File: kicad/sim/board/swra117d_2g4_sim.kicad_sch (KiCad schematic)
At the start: 2 parts, among them P1 50R port

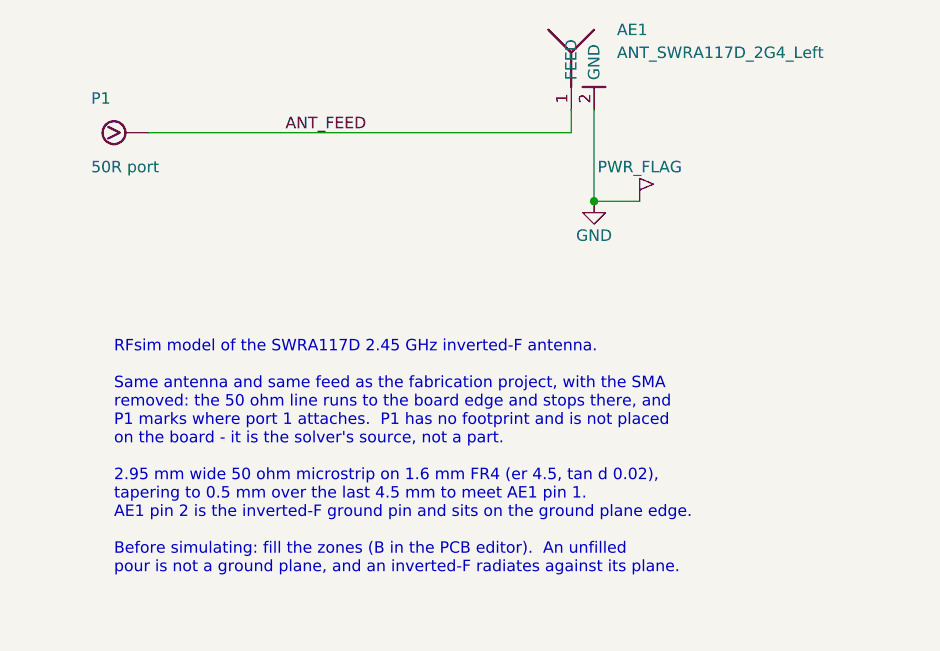
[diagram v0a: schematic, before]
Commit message: Give the RFsim port a pad with reference copper under it
RFsim reported, on the previous version:

    Port 1 (AE1 Pad 1 (ANT_FEED)): no copper on reference layer B.Cu under
    the pad.

Two things behind it, and the first one was my mistake.  RFsim attaches its
port to a *pad*, not to a track end, so removing the connector left the board
with no pad at the launch and RFsim fell back to the antenna's own feed pad -
which sits on the ground plane edge with the keep-out above it and has no
plane beneath it by design.  A bare track end was never going to work.

So the connector is replaced by a bare port land rather than by nothing:

  * RF_Port_Land - the signal pad, the width of the 50 ohm line, with a solid
    B.Cu ground pad directly under it.  Generated by gen_sma_footprint.py
    --style port, from the same code and the same stackup as the SMA land, so
    the only electrical difference between the two boards is the thing being
    measured.
  * No coplanar ground tabs.  That is what keeps the line a plain microstrip,
    and it is why MSL is the right port model here where CPW is right on the
    fabrication board.  check_sim_board.py fails if anyone adds an F.Cu ground
    pad back, because that silently invalidates the port model the docs tell
    you to use.
  * The reference is a pad, not a zone.  Zones ship unfilled, so a reference
    that waits on a fill is a reference that is missing the first time the
    project is opened - which is the second half of the reported error.

RF_PORT gains a ground pin and the RF_Port_Land footprint; P1 is now a real
board part rather than a sheet-only symbol.  The feed line ends on the port
pad instead of the board edge.  Launch vias sit inside the land's ground pad.

Also fixed: gen_sma_footprint.py derived three uuids from hash(), which
Python salts per process, so the footprint came out different on every run.
Numbered instead.  The fabrication board changes by three uuids and no
geometry.

check_sim_board.py grows t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
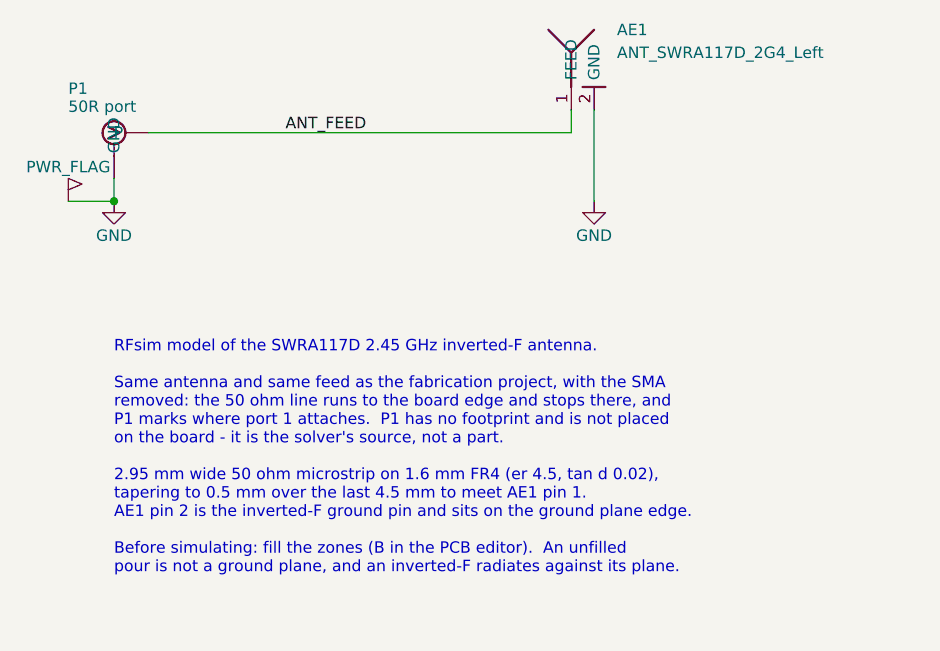
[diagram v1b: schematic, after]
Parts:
- P1: footprint (none) -> SWRA117D_RF:RF_Port_Land
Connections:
- net GND: now also P1.2 (GND)
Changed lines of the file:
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@@
+	)
+	(wire
+		(pts (xy 76.2 93.98) (xy 76.2 96.52))
+		(stroke (width 0) (type default))
+	)
+	(wire
+		(pts (xy 76.2 96.52) (xy 71.12 96.52))
+		(stroke (width 0) (type default))
 	)
 	(wire
@@
 		(stroke (width 0) (type default))
 	)
-	(wire
-		(pts (xy 129.54 96.52) (xy 134.62 96.52))
-		(stroke (width 0) (type default))
-	)
 	(junction
-		(at 129.54 96.52)
+		(at 76.2 96.52)
 		(diameter 0)
 		(color 0 0 0 0)
@@
 		(exclude_from_sim no)
 		(in_bom no)
-		(on_board no)
+		(on_board yes)
 		(dnp no)
-		(property "Reference" "P1"
-			(at 73.66 85.09 0)
-			(effects (font (size 1.27 1.27)) (justify left))
+		(property "Reference" "P1" (at 71.12 84 0) (effects (font (size 1.27 1.27)) (justify left)))
+		(property "Value" "50R port" (at 71.12 86 0) (effects (font (size 1.27 1.27)) (justify left)))
+		(property "Footprint" "SWRA117D_RF:RF_Port_Land"
+			(at 76.2 88.9 0)
+			(effects (font (size 1.27 1.27)) (hide yes))
 		)
-		(property "Value" "50R port"
-			(at 73.66 92.71 0)
-			(effects (font (size 1.27 1.27)) (justify left))
-		)
-		(property "Footprint" "" (at 76.2 88.9 0) (effects (font (size 1.27 1.27)) (hide yes)))
 		(property "Datasheet" "~" (at 76.2 88.9 0) (effects (font (size 1.27 1.27)) (hide yes)))
-		(property "Description" "50 ohm simulation port - attach RFsim port 1 to the feed track where it meets the board edge"
+		(property "Description" "50 ohm board-edge port land - attach RFsim port 1 to pad 1, with pad 2 on B.Cu as its reference"
 			(at 76.2 88.9 0)
 			(effects (font (size 1.27 1.27)) (hide yes))
 		)
 		(pin "1")
+		(pin "2")
 		(instances
 			(project "swra117d_2g4_sim"
@@
 	(symbol
 		(lib_id "SWRA117D_RF:GND")
+		(at 76.2 96.52 0)
+		(unit 1)
+		(exclude_from_sim no)
+		(in_bom yes)
+		(on_board yes)
+		(dnp no)
+		(property "Reference" "#PWR01"
+			(at 76.2 102.87 0)
+			(effects (font (size 1.27 1.27)) (hide yes))
+		)
+		(property "Value" "GND" (at 76.2 100.33 0) (effects (font (size 1.27 1.27))))
+		(property "Footprint" "" (at 76.2 96.52 0) (effects (font (size 1.27 1.27)) (hide yes)))
+		(property "Datasheet" "" (at 76.2 96.52 0) (effects (font (size 1.27 1.27)) (hide yes)))
+		(property "Description" "Ground reference"
+			(at 76.2 96.52 0)
+			(effects (font (size 1.27 1.27)) (hide yes))
+		)
+		(pin "1")
+		(instances
+			(project "swra117d_2g4_sim"
+				(path "/f0820ba2-7329-58cb-a18e-f65c6c3dd98c" (reference "#PWR01") (unit 1))
+			)
+		)
+	)
+	(symbol
+		(lib_id "SWRA117D_RF:GND")
 		(at 129.54 96.52 0)
 		(unit 1)
@@
 		(on_board yes)
 		(dnp no)
-		(property "Reference" "#PWR01"
+		(property "Reference" "#PWR02"
 			(at 129.54 102.87 0)
 			(effects (font (size 1.27 1.27)) (hide yes))
@@
 		(instances
 			(project "swra117d_2g4_sim"
-				(path "/f0820ba2-7329-58cb-a18e-f65c6c3dd98c" (reference "#PWR01") (unit 1))
+				(path "/f0820ba2-7329-58cb-a18e-f65c6c3dd98c" (reference "#PWR02") (unit 1))
 			)
 		)
@@
 	(symbol
 		(lib_id "SWRA117D_RF:PWR_FLAG")
-		(at 134.62 96.52 0)
+		(at 71.12 96.52 0)
 		(unit 1)
 		(exclude_from_sim yes)
@@
 		(dnp no)
 		(property "Reference" "#FLG01"
-			(at 134.62 102.87 0)
+			(at 71.12 102.87 0)
 			(effects (font (size 1.27 1.27)) (hide yes))
 		)
-		(property "Value" "PWR_FLAG" (at 134.62 92.71 0) (effects (font (size 1.27 1.27))))
-		(property "Footprint" "" (at 134.62 96.52 0) (effects (font (size 1.27 1.27)) (hide yes)))
-		(property "Datasheet" "" (at 134.62 96.52 0) (effects (font (size 1.27 1.27)) (hide yes)))
+		(property "Value" "PWR_FLAG" (at 71.12 92.71 0) (effects (font (size 1.27 1.27))))
+		(property "Footprint" "" (at 71.12 96.52 0) (effects (font (size 1.27 1.27)) (hide yes)))
+		(property "Datasheet" "" (at 71.12 96.52 0) (effects (font (size 1.27 1.27)) (hide yes)))
 		(property "Description" "ERC power source flag"
-			(at 134.62 96.52 0)
+			(at 71.12 96.52 0)
 			(effects (font (size 1.27 1.27)) (hide yes))
 		)

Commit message: RFsim project: ground on layer 2 only, as SWRA117D Figure 3 draws it
Figure 3 is a two layer board where layer 1 carries the antenna and the feed
and the ground is the grey area captioned "Ground Layer 2" - layer 2 and
nowhere else.  There is no ground copper on the top layer at all, and exactly
one via in the whole drawing: "Via to ground", the W1 = 0.90 mm pad that
shorts the inverted-F.  The simulation project is now that arrangement.  The
fabrication project, with its SMA, is untouched.

One change, three arguments settled:

  * no coplanar copper anywhere near the line, so the feed is unambiguously a
    microstrip over layer 2 and MSL is the port model with nothing left to
    debate;
  * no top pour, so no pour islands to resonate and nothing to stitch - the
    board's only via is the antenna's own, which is what the figure shows;
  * the port's reference is the plane itself, directly under the signal pad,
    rather than a second sheet of copper that has to be tied to it.

The openEMS model reads which layers actually carry ground and builds only
those: it had been adding a top pour unconditionally, which on this board
would have turned the feed into a coplanar line and answered a different
question than the figure asks.

check_sim_board.py now fails on a pour outside B.Cu, on any via at all (the
antenna's ground pad is a pad, not a via), and on that pad ceasing to be a
plated through hole - Figure 3's short.  plane_edge returns None rather than
throwing when a board has no pour, so a deleted plane is reported instead of
crashing the checker; mutate_sim_board.py counts that case as CRASHED, not
caught, which is how it was found.  18 mutations, 18 caught.
stitching_span.py reports "nothing to stitch" for a single-layer ground
instead of aborting.

Co-Authored-By: Claude Opus 5 <noreply@anthropic.com>
Claude-Session: https://claude.ai/code/session_01Prj6bUQ2KQzzxzD4bgtswJ
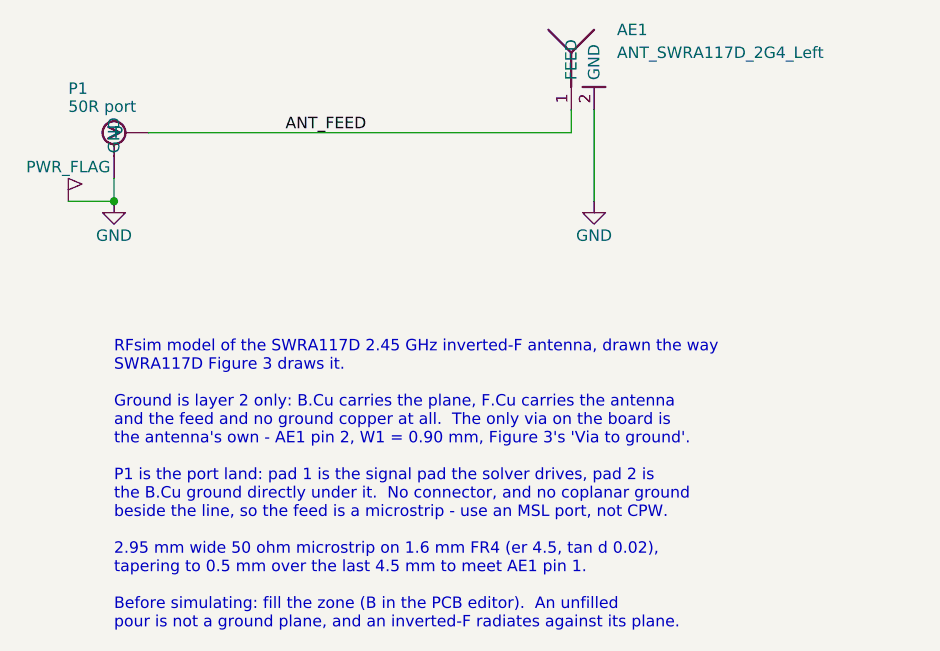
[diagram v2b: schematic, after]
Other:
- note added: "RFsim model of the SWRA117D 2.45 GHz inverted-F antenna, drawn the way SWRA117D Figure 3 draws it. Ground is layer 2 only: B.Cu carries the plane, F.Cu carries the antenna and the feed and no ground copper at all. The only via on the board is the antenna's own - AE1 pin 2, W1 = 0.90 mm, Figure 3's 'Via to ground'. P1 is the port land: pad 1 is the signal pad the solver drives, pad 2 is the B.Cu g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"
- note removed: "RFsim model of the SWRA117D 2.45 GHz inverted-F antenna. Same antenna and same feed as the fabrication project, with the SMA removed: the 50 ohm line runs to the board edge and stops there, and P1 marks where port 1 attaches. P1 has no footprint and is not placed on the board - it is the solver's source, not a part. 2.95 mm wide 50 ohm microstrip on 1.6 mm FR4 (er 4.5, tan d 0.02), tapering to 0.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"
- title: SWRA117D 2.45 GHz IFA - RFsim model: antenna + 50 ohm feed, no connector -> SWRA117D 2.45 GHz IFA - RFsim model per Figure 3: ground on layer 2, direct feed, no connector
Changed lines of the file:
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@@
 	(paper "A4")
 	(title_block
-		(title "SWRA117D 2.45 GHz IFA - RFsim model: antenna + 50 ohm feed, no connector")
+		(title "SWRA117D 2.45 GHz IFA - RFsim model per Figure 3: ground on layer 2, direct feed, no connector"
+		)
 		(date "2026-09-12")
 		(rev "A")
@@
 		(effects (font (size 1.27 1.27)) (justify left bottom))
 	)
-	(text "RFsim model of the SWRA117D 2.45 GHz inverted-F antenna.\n\nSame antenna and same feed as the fabrication project, with the SMA\nremoved: the 50 ohm line runs to the board edge and stops there, and\nP1 marks where port 1 attaches.  P1 has no footprint and is not placed\non the board - it is the solver's source, not a part.\n\n2.95 mm wide 50 ohm microstrip on 1.6 mm FR4 (er 4.5, tan d 0.02),\ntapering to 0.5 mm over the last 4.5 mm to meet AE1 pin 1.\nAE1 pin 2 is the inverted-F ground pin and sits on the ground plane edge.\n\nBefore simulating: fill the zones (B in the PCB editor).  An unfilled\npour is not a ground plane, and an inverted-F radiates against its plane."
+	(text "RFsim model of the SWRA117D 2.45 GHz inverted-F antenna, drawn the way\nSWRA117D Figure 3 draws it.\n\nGround is layer 2 only: B.Cu carries the plane, F.Cu carries the antenna\nand the feed and no ground copper at all.  The only via on the board is\nthe antenna's own - AE1 pin 2, W1 = 0.90 mm, Figure 3's 'Via to ground'.\n\nP1 is the port land: pad 1 is the signal pad the solver drives, pad 2 is\nthe B.Cu ground directly under it.  No connector, and no coplanar ground\nbeside the line, so the feed is a microstrip - use an MSL port, not CPW.\n\n2.95 mm wide 50 ohm microstrip on 1.6 mm FR4 (er 4.5, tan d 0.02),\ntapering to 0.5 mm over the last 4.5 mm to meet AE1 pin 1.\n\nBefore simulating: fill the zone (B in the PCB editor).  An unfilled\npour is not a ground plane, and an inverted-F radiates against its plane."
 		(exclude_from_sim no)
 		(at 76.2 112 0)
